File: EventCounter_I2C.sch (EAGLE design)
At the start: 32 parts, among them J1 CONN_42.54_SCREW, J2 CONN_32.54_SCREW, Q3 DMG3404, U1 TLV3691DCK, U11 SN74AUP3G34DCU, U12 TXS0102DQM, U2 TPS7A0533DBV, U7 ATTINY441/841VQFN, U8 SN74AUP1G34SC70

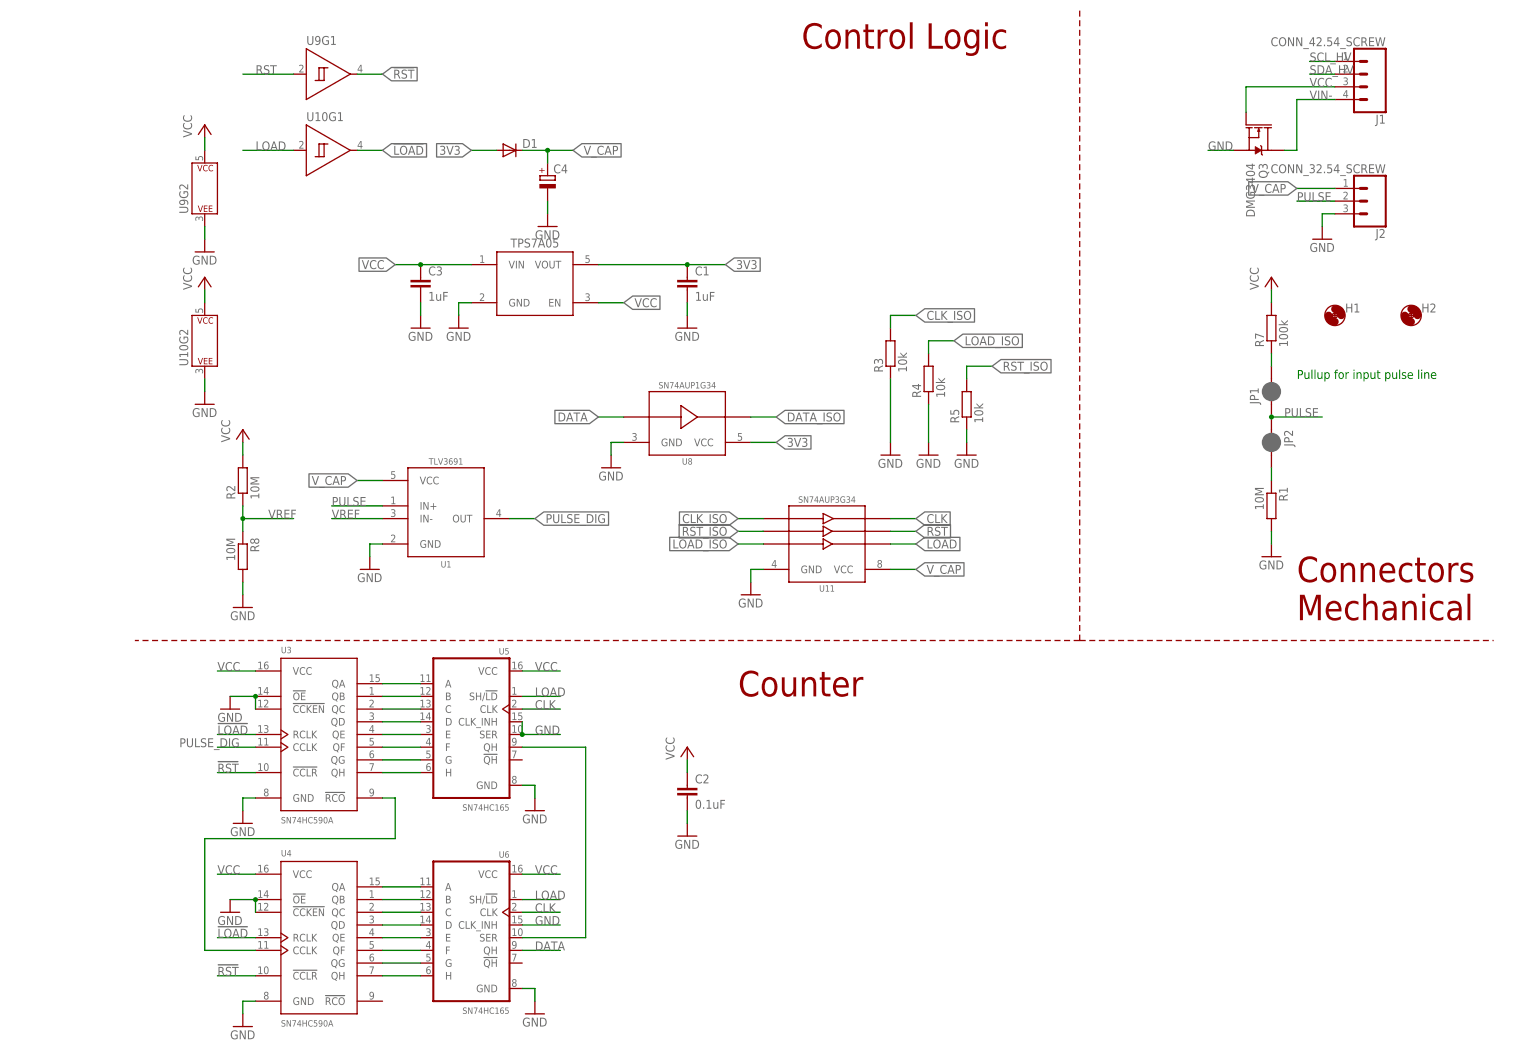
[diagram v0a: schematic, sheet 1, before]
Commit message: Initial layout for I2C variant
First cut layout for I2C variant, passes DRC, still needs verification
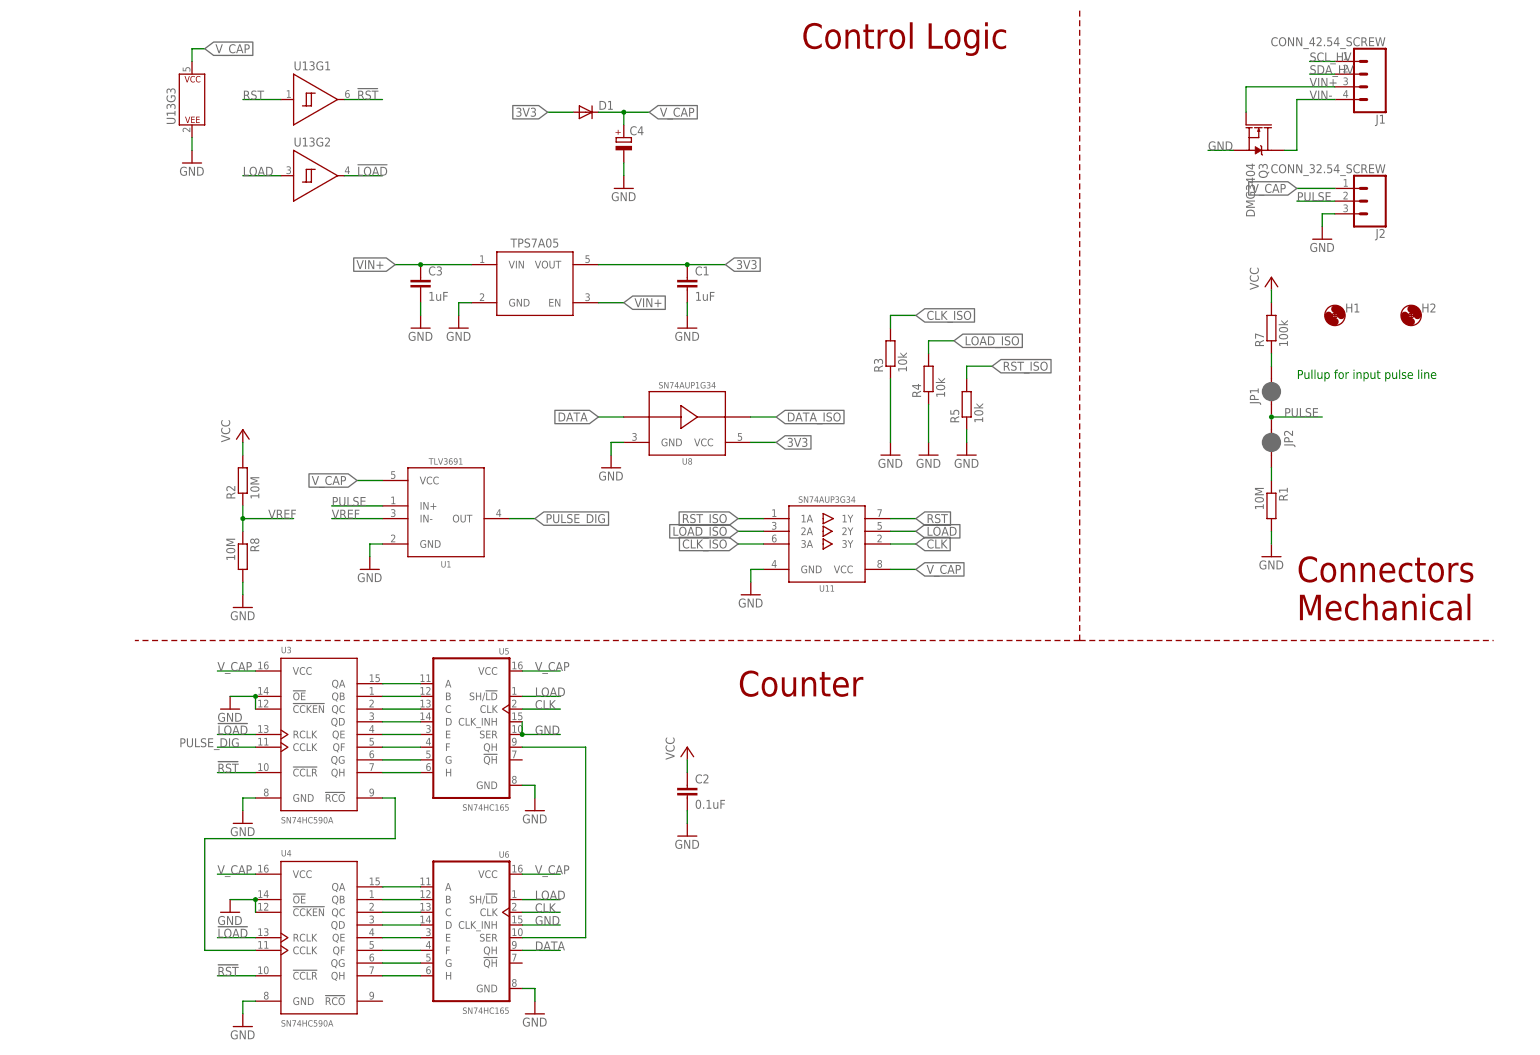
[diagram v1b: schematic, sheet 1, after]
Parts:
- removed U10, U9: (no value), bschulz:SN74LVC1G14DCK
- added C5: (no value), bschulz_passives:C-EU0.1UFC0402
- added U13: (no value), bschulz:SN74AUP2G14SC70
- C2: device bschulz_passives:C-EU0.1UFC0603 -> bschulz_passives:C-EU0.1UFC0402
- U5, U6: device bschulz:SN74HC165D -> bschulz:SN74HC165PW
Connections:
- removed net VCC: C2.1, C3.1, J1.3, Q3.G, R2.2, R7.2, U10G2.P$V+, U12.VB, U2.EN, U2.VIN, U3.VCC, U4.VCC, U5.VCC, U6.VCC, U9G2.P$V+
- new net VIN+: C3.1, J1.3, Q3.G, U12.VB, U2.EN, U2.VIN
- net !LOAD: now also U13G2.Y; no longer U10G1.Y
- net !RST: now also U13G1.Y; no longer U9G1.Y
- net 3V3: now also C5.1
- net CLK: now also U11.3Y; no longer U11.1Y
- net CLK_ISO: now also U11.3A, U7.PA1; no longer U11.1A
- net DATA_ISO: now also U7.PA0
- net GND: now also C5.2, U13G3.P$V-; no longer U10G2.P$V-, U9G2.P$V-
- net LOAD: now also U11.2Y, U13G2.A; no longer U10G1.A, U11.3Y
- net LOAD_ISO: now also U11.2A, U7.PA3; no longer U11.3A
- net RST: now also U11.1Y, U13G1.A; no longer U11.2Y, U9G1.A
- net RST_ISO: now also U11.1A, U7.PA2; no longer U11.2A
- net V_CAP: now also C2.1, R2.2, R7.2, U13G3.P$V+, U3.VCC, U4.VCC, U5.VCC, U6.VCC
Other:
- moved on the sheet: C4, D1

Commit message: Minor edits, sent to fab for v1.0 (I2C model)
Cleaned up layout, added pullup reset resistor, generated gerbers, sent v1.0 to fab
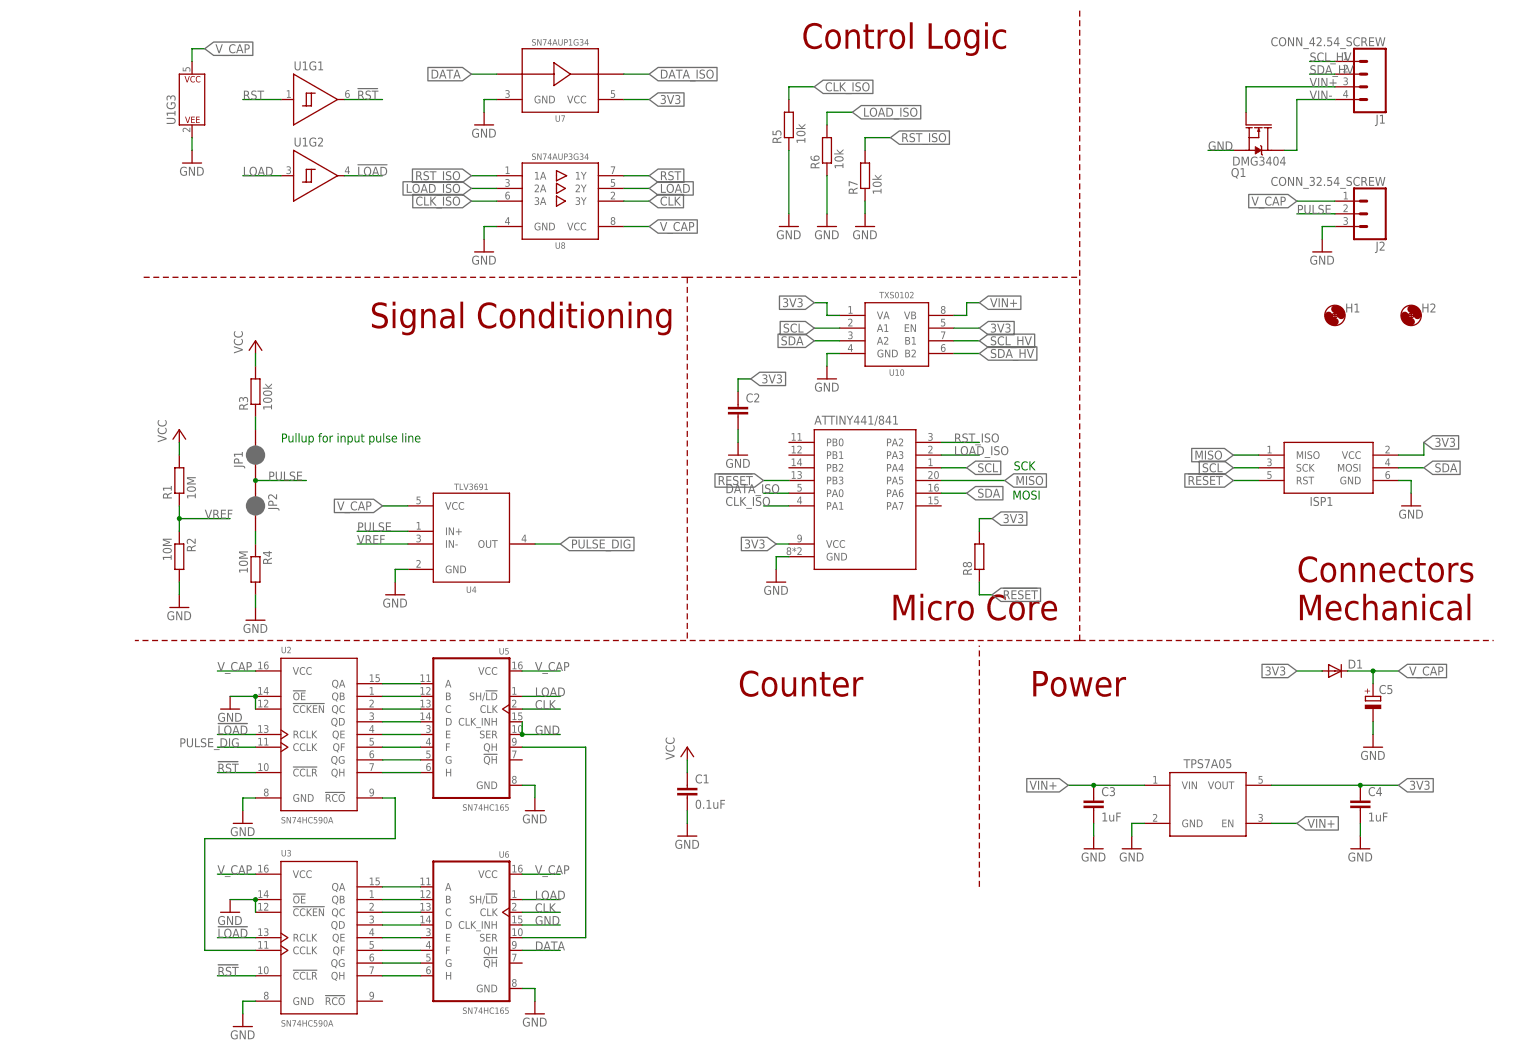
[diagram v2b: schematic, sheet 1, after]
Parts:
- removed U12: TXS0102DQM, bschulz:TXS0102DQM
- removed U13: (no value), bschulz:SN74AUP2G14SC70
- added R6: 10k, bschulz_passives:R-EU_10KR0402
- added U10: TXS0102DQM, bschulz:TXS0102DQM
- added U9: ATTINY441/841VQFN, bschulz:ATTINY441/841VQFN
- C1: value 1uF -> 0.1uF; device bschulz_passives:C-EU1UFC0603 -> bschulz_passives:C-EU0.1UFC0402
- C2: value 0.1uF -> (none)
- C4: value (none) -> 1uF; device bschulz_passives:CPOL-EUHL -> bschulz_passives:C-EU1UFC0603
- C5: device bschulz_passives:C-EU0.1UFC0402 -> bschulz_passives:CPOL-EUHL
- R3: value 10k -> 100k; device bschulz_passives:R-EU_10KR0402 -> bschulz_passives:R-EU_R0603
- R4: value 10k -> 10M; device bschulz_passives:R-EU_10KR0402 -> bschulz_passives:R-EU_10MR0603
- R7: value 100k -> 10k; device bschulz_passives:R-EU_R0603 -> bschulz_passives:R-EU_10KR0402
- R8: value 10M -> (none); device bschulz_passives:R-EU_10MR0603 -> bschulz_passives:R-EU_10KR0402
- U1: value TLV3691DCK -> (none); device bschulz:TLV3691DCK -> bschulz:SN74AUP2G14SC70
- U11: value SN74AUP3G34DCU -> TPS7A0533DBV; device bschulz:SN74AUP3G34DCU -> bschulz:TPS7A0533DBV
- U2: value TPS7A0533DBV -> (none); device bschulz:TPS7A0533DBV -> bschulz:SN74HC590AD
- U4: value (none) -> TLV3691DCK; device bschulz:SN74HC590AD -> bschulz:TLV3691DCK
- U7: value ATTINY441/841VQFN -> SN74AUP1G34SC70; device bschulz:ATTINY441/841VQFN -> bschulz:SN74AUP1G34SC70
- U8: value SN74AUP1G34SC70 -> SN74AUP3G34DCU; device bschulz:SN74AUP1G34SC70 -> bschulz:SN74AUP3G34DCU
- renumbered Q3 to Q1
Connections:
- net !LOAD: now also U1G2.Y, U2.RCLK; no longer U13G2.Y, U4.RCLK
- net !RESET: now also R8.1, U9.PB3; no longer U7.PB3
- net !RST: now also U1G1.Y, U2.!CCLR; no longer U13G1.Y, U4.!CCLR
- net 3V3: now also C2.1, C4.1, R8.2, U10.EN, U10.VA, U11.VOUT, U9.VCC; no longer C1.1, C5.1, U12.EN, U12.VA, U2.VOUT, U8.VCC
- net CLK: now also U8.3Y; no longer U11.3Y
- net CLK_ISO: now also R5.2, U8.3A, U9.PA1; no longer R3.2, U11.3A, U7.PA1
- net DATA: now also U7.A; no longer U8.A
- net DATA_ISO: now also U7.Y, U9.PA0; no longer U7.PA0, U8.Y
- net GND: now also C4.2, C5.-, R2.2, R4.2, R6.1, R7.1, U10.GND, U1G3.P$V-, U2.!CCKEN, U2.!OE, U9.GND; no longer C4.-, C5.2, R1.2, R3.1, R4.1, R8.2, U1.GND, U12.GND, U13G3.P$V-, U4.!CCKEN, U4.!OE
- net LOAD: now also U1G2.A, U8.2Y; no longer U11.2Y, U13G2.A
- net LOAD_ISO: now also R6.2, U8.2A, U9.PA3; no longer R4.2, U11.2A, U7.PA3
- net MISO: now also U9.PA5; no longer U7.PA5
- net N$1: now also U3.QA; no longer U4.QA
- net N$10: now also U2.QG; no longer U3.QG
- net N$11: now also U2.QF; no longer U3.QF
- net N$12: now also U2.QE; no longer U3.QE
- net N$13: now also U2.QD; no longer U3.QD
- net N$14: now also U2.QC; no longer U3.QC
- net N$15: now also U2.QB; no longer U3.QB
- net N$16: now also U2.QA; no longer U3.QA
- net N$18: now also U2.!RCO, U3.CCLK; no longer U3.!RCO, U4.CCLK
- net N$19: now also R4.1; no longer R1.1
- net N$2: now also U3.QB; no longer U4.QB
- net N$20: now also R3.1; no longer R7.1
- net N$3: now also U3.QC; no longer U4.QC
- net N$4: now also U3.QD; no longer U4.QD
- net N$5: now also U3.QE; no longer U4.QE
- net N$6: now also U3.QF; no longer U4.QF
- net N$7: now also U3.QG; no longer U4.QG
- net N$8: now also U3.QH; no longer U4.QH
- net N$9: now also U2.QH; no longer U3.QH
- net PULSE: now also U4.IN+; no longer U1.IN+
- net PULSE_DIG: now also U2.CCLK, U4.OUT; no longer U1.OUT, U3.CCLK
- net RST: now also U1G1.A, U8.1Y; no longer U11.1Y, U13G1.A
- net RST_ISO: now also R7.2, U8.1A, U9.PA2; no longer R5.2, U11.1A, U7.PA2
- net SCL: now also U10.A1, U9.PA4; no longer U12.A1, U7.PA4
- net SCL_HV: now also U10.B1; no longer U12.B1
- net SDA: now also U10.A2, U9.PA6; no longer U12.A2, U7.PA6
- net SDA_HV: now also U10.B2; no longer U12.B2
- net VIN+: now also U10.VB, U11.EN, U11.VIN; no longer U12.VB, U2.EN, U2.VIN
- net VREF: now also R1.1, U4.IN-; no longer R8.1, U1.IN-
- net V_CAP: now also C1.1, C5.+, R1.2, R3.2, U1G3.P$V+, U2.VCC, U8.VCC; no longer C2.1, C4.+, R2.2, R7.2, U1.VCC, U11.VCC, U13G3.P$V+
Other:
- note added: "Micro Core"
- note added: "Power"
- note added: "Signal Conditioning"
- note removed: "Connect: LOAD_ISO RST_ISO CLK_ISO DATA_ISO"
- moved on the sheet: C1, C2, C3, D1, J2, JP1, JP2, R1, R2, R3, R4, R5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
